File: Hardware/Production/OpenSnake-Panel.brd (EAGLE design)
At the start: 25.4 x 69.8 mm, 54 parts, among them Q1 16MHZ, U1 ATMEGA328P, U2 317

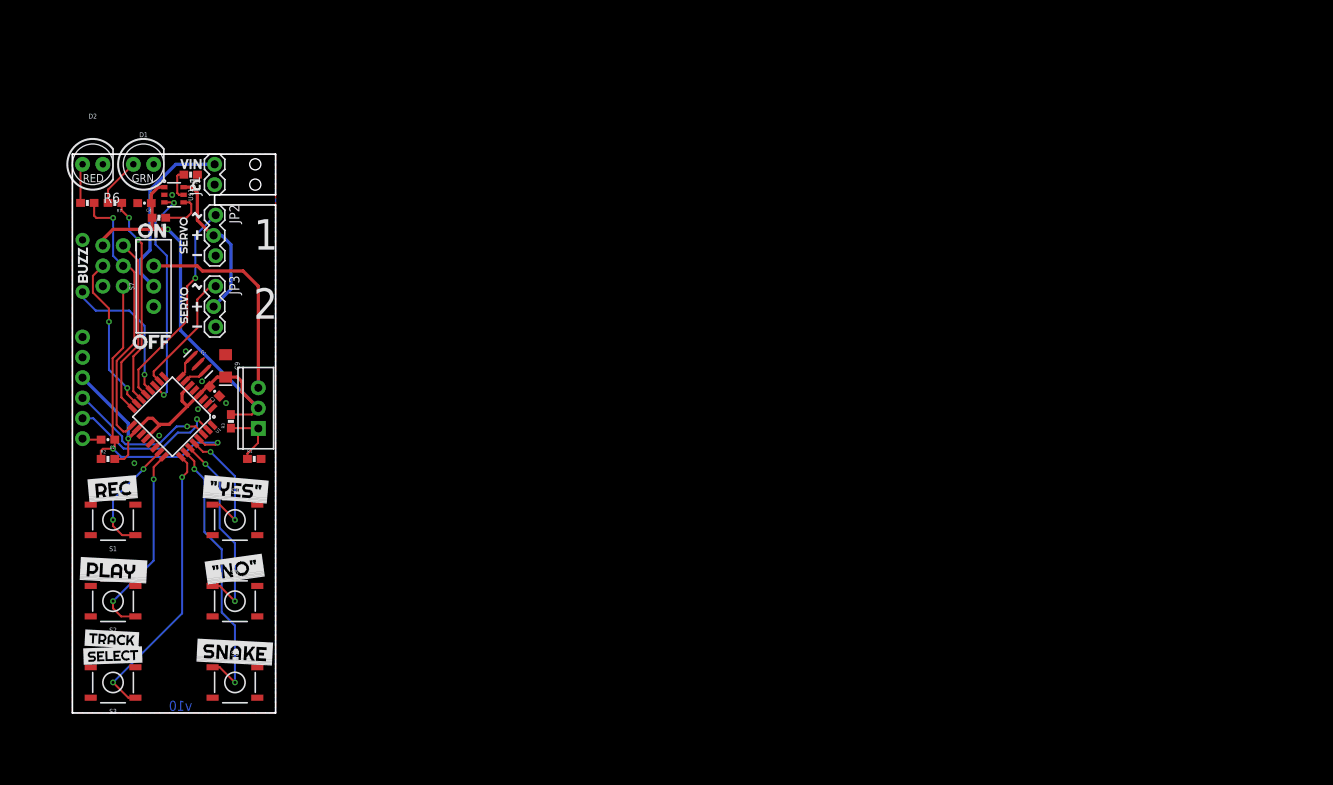
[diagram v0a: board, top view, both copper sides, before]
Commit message: final changes to v10
-added green LED
-added silk labels for servo ports
-Panelized and cammed
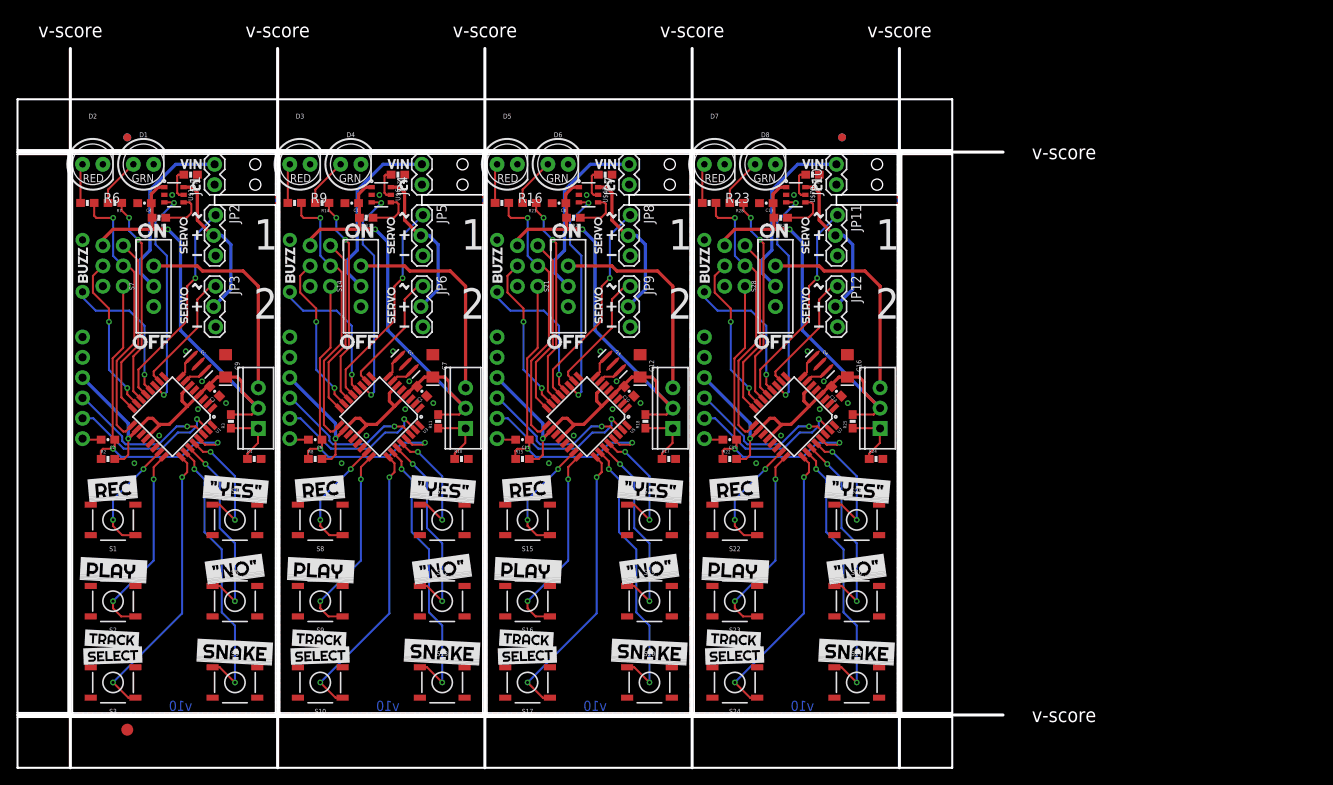
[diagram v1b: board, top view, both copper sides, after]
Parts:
- removed FRAME1: FRAME-LETTER, SparkFun-Aesthetics:CREATIVE_COMMONS
- added C1, C10, C11, C13, C14, C15, C5, C6, C8: 0.1uF, SparkFun-Capacitors:0603-CAP
- added C12, C16, C7: 10uF, SparkFun-Capacitors:EIA3216
- added D3, D5, D7: RED, SparkFun-LED:LED_5MM
- added D4, D6, D8: GREEN, SparkFun-LED:LED_5MM
- added E$1, E$2, E$3, E$4: (no value), SparkFun-Aesthetics:FIDUCIAL-1X2
- added E$5: (no value), SparkFun-Retired:FIDUCIAL-1.5X3
- added J3, J5, J7: (no value), SparkFun-Connectors:6_PIN_SERIAL_TARGET_SIDE_W_SILK
- added J4, J6, J8: (no value), SparkFun-Connectors:2X3
- added JP10, JP4, JP7: (no value), Testing:1X02
- added JP11, JP5, JP8: Servo 1, Testing:1X03_LOCK
- added JP12, JP6, JP9: Servo 2, Testing:1X03_LOCK
- added LOGO2, LOGO3, LOGO4: OSHW-LOGOL, SparkFun-Aesthetics:OSHW-LOGO-L
- added LS2, LS3, LS4: BUZZER, SparkFun-Electromechanical:BUZZER-12MM
- added Q2, Q3, Q4: 16MHZ, SparkFun-FreqCtrl:RESONATOR-SMD
- added R10, R17, R24: 715, SparkFun-Resistors:0603-RES
- added R11, R18, R25: 240, SparkFun-Resistors:0603-RES
- added R12, R13, R15, R19, R20, R22, R26, R27, R8: 10K, SparkFun-Resistors:0603-RES
- added R14, R16, R21, R23, R28, R9: 330, SparkFun-Resistors:0603-RES
- added S10, S11, S12, S13, S15, S16, S17, S18, S19, S20, S22, S23, S24, S25, S26, S27, S8, S9: (no value), SparkFun-Switches:TACTILE_SWITCH_SMD_5.2MM
- added S14, S21, S28: (no value), SparkFun-Switches:SWITCH_SPDT_PTH_11.6X4.0MM
- added U$25, U$48, U$71: (no value), buzzard_labels:#YES#0
- added U$26, U$49, U$72: (no value), buzzard_labels:#NO#1
- added U$27, U$50, U$73: (no value), buzzard_labels:SNAKE2
- added U$28, U$51, U$74: (no value), buzzard_labels (1):ON0
- added U$29, U$52, U$75: (no value), buzzard_labels (1):OFF1
- added U$30, U$53, U$76: (no value), buzzard_labels (1):VIN6
- added U$31, U$54, U$77: (no value), buzzard_labels (1):G8
- added U$32, U$55, U$78: (no value), buzzard_labels (2):REC0
- added U$33, U$56, U$79: (no value), buzzard_labels (2):PLAY_1
- added U$34, U$57, U$80: (no value), buzzard_labels (2):TRACK2
- added U$35, U$58, U$81: (no value), buzzard_labels (2):SELECT3
- added U$36, U$59, U$82: (no value), snake:MARIO_LOGO
- added U$37, U$60, U$83: (no value), buzzard_labels (4):BUZZ0
- added U$38, U$39, U$61, U$62, U$84, U$85: (no value), buzzard_labels (6):#1
- added U$40, U$41, U$63, U$64, U$86, U$87: (no value), buzzard_labels (6):SERVO2
- added U$42, U$65, U$88: (no value), buzzard_labels (7):SNAKE0
- added U$43, U$66, U$89: (no value), buzzard_labels (7):IN1
- added U$44, U$67, U$90: (no value), buzzard_labels (7):A2
- added U$45, U$68, U$91: (no value), buzzard_labels (7):CAN3
- added U$46, U$69, U$92: (no value), buzzard_labels (7):CONTROLLER4
- added U$47, U$6, U$70: (no value), snake:SOT26
- added U3, U5, U7: ATMEGA328P, SparkFun-DigitalIC:TQFP32-08
- added U4, U6, U8: 317, SparkFun-IC-Power:TO220-ADJ
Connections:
- new net !DTR1: C6.2, J3.P$1
- new net !DTR2: C11.2, J5.P$1
- new net !DTR3: C15.2, J7.P$1
- new net BUZZER1: LS2.+, U3.12
- new net BUZZER2: LS3.+, U5.12
- new net BUZZER3: LS4.+, U7.12
- new net D1: U3.32
- new net D3: U5.32
- new net D4: U7.32
- new net ENABLE_SERVO1: U$6.3, U3.11
- new net ENABLE_SERVO2: U$47.3, U5.11
- new net ENABLE_SERVO3: U$70.3, U7.11
- new net GND1: C1.2, C5.1, C7.-, D3.K, D4.K, J3.P$5, J3.P$6, J4.6, JP4.1, JP5.3, JP6.3, LS2.-, Q2.2, R10.2, R12.1, S10.3, S11.3, S12.3, S13.3, S8.3, S9.3, U$6.2, U3.21, U3.3, U3.5
- new net GND2: C10.1, C12.-, C8.2, D5.K, D6.K, J5.P$5, J5.P$6, J6.6, JP7.1, JP8.3, JP9.3, LS3.-, Q3.2, R17.2, R19.1, S15.3, S16.3, S17.3, S18.3, S19.3, S20.3, U$47.2, U5.21, U5.3, U5.5
- new net GND3: C13.2, C14.1, C16.-, D7.K, D8.K, J7.P$5, J7.P$6, J8.6, JP10.1, JP11.3, JP12.3, LS4.-, Q4.2, R24.2, R26.1, S22.3, S23.3, S24.3, S25.3, S26.3, S27.3, U$70.2, U7.21, U7.3, U7.5
- new net GRN_LED1: R14.1, U3.14
- new net GRN_LED2: R21.1, U5.14
- new net GRN_LED3: R28.1, U7.14
- new net MISO1: J4.1, U3.16
- new net MISO2: J6.1, U5.16
- new net MISO3: J8.1, U7.16
- new net MOSI1: J4.4, U3.15
- new net MOSI2: J6.4, U5.15
- new net MOSI3: J8.4, U7.15
- new net N$11: D3.A, R9.2
- new net N$12: Q2.1, U3.8
- new net N$13: Q2.3, U3.7
- new net N$14: R10.1, R11.1, U4.ADJ
- new net N$15: JP4.2, S14.2
- new net N$16: S14.1, U4.IN
- new net N$17: JP5.2, JP6.2, U$6.6
- new net N$18: R12.2, U$6.5
- new net N$19: R13.1, U$6.4
- new net N$20: D4.A, R14.2
- new net N$21: D5.A, R16.2
- new net N$22: Q3.1, U5.8
- new net N$23: Q3.3, U5.7
- new net N$24: R17.1, R18.1, U6.ADJ
- new net N$25: JP7.2, S21.2
- new net N$26: S21.1, U6.IN
- new net N$27: JP8.2, JP9.2, U$47.6
- new net N$28: R19.2, U$47.5
- new net N$29: R20.1, U$47.4
- new net N$30: D6.A, R21.2
- new net N$31: D7.A, R23.2
- new net N$32: Q4.1, U7.8
- new net N$33: Q4.3, U7.7
- new net N$34: R24.1, R25.1, U8.ADJ
- new net N$35: JP10.2, S28.2
- new net N$36: S28.1, U8.IN
- new net N$37: JP11.2, JP12.2, U$70.6
- new net N$38: R26.2, U$70.5
- new net N$39: R27.1, U$70.4
- new net N$40: D8.A, R28.2
- new net NO1: S12.1, U3.27
- new net NO2: S19.1, U5.27
- new net NO3: S26.1, U7.27
- new net PLAY1: S9.1, U3.24
- new net PLAY2: S16.1, U5.24
- new net PLAY3: S23.1, U7.24
- new net REC1: S8.1, U3.23
- new net REC2: S15.1, U5.23
- new net REC3: S22.1, U7.23
- new net RST1: C6.1, J4.5, R8.1, U3.29
- new net RST2: C11.1, J6.5, R15.1, U5.29
- new net RST3: C15.1, J8.5, R22.1, U7.29
- new net RX1: J3.P$3, U3.30
- new net RX2: J5.P$3, U5.30
- new net RX3: J7.P$3, U7.30
- new net SCK1: J4.3, R9.1, U3.17
- new net SCK2: J6.3, R16.1, U5.17
- new net SCK3: J8.3, R23.1, U7.17
- new net SERVO_3: JP5.1, U3.13
- new net SERVO_4: JP6.1, U3.10
- new net SERVO_5: JP8.1, U5.13
- new net SERVO_6: JP9.1, U5.10
- new net SERVO_7: JP11.1, U7.13
- new net SERVO_8: JP12.1, U7.10
- new net SNAKE1: S13.1, U3.26
- new net SNAKE2: S20.1, U5.26
- new net SNAKE3: S27.1, U7.26
- new net TRCK_SEL1: S10.1, U3.25
- new net TRCK_SEL2: S17.1, U5.25
- new net TRCK_SEL3: S24.1, U7.25
- new net TX1: J3.P$2, U3.31
- new net TX2: J5.P$2, U5.31
- new net TX3: J7.P$2, U7.31
- new net VCC1: C1.1, C5.2, C7.+, J3.P$4, J4.2, R11.2, R13.2, R8.2, U$6.1, U3.18, U3.20, U3.4, U3.6, U4.OUT
- new net VCC2: C10.2, C12.+, C8.1, J5.P$4, J6.2, R15.2, R18.2, R20.2, U$47.1, U5.18, U5.20, U5.4, U5.6, U6.OUT
- new net VCC3: C13.1, C14.2, C16.+, J7.P$4, J8.2, R22.2, R25.2, R27.2, U$70.1, U7.18, U7.20, U7.4, U7.6, U8.OUT
- new net YES1: S11.1, U3.28
- new net YES2: S18.1, U5.28
- new net YES3: S25.1, U7.28
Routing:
- net VCC3: track 0.00 -> 91.3 mm, vias 0 -> 2
- net VCC2: track 0.00 -> 91.3 mm, vias 0 -> 2
- net VCC1: track 0.00 -> 91.3 mm, vias 0 -> 2
- net RST3: track 0.00 -> 40.7 mm, vias 0 -> 2
- net RST2: track 0.00 -> 40.7 mm, vias 0 -> 2
- net RST1: track 0.00 -> 40.7 mm, vias 0 -> 2
- net TRCK_SEL3: track 0.00 -> 36.0 mm, vias 0 -> 2
- net TRCK_SEL2: track 0.00 -> 36.0 mm, vias 0 -> 2
- net TRCK_SEL1: track 0.00 -> 36.0 mm, vias 0 -> 2
- net SCK3: track 0.00 -> 35.0 mm, vias 0 -> 1
- net SCK2: track 0.00 -> 35.0 mm, vias 0 -> 1
- net SCK1: track 0.00 -> 35.0 mm, vias 0 -> 1
- net SNAKE1: track 0.00 -> 34.9 mm, vias 0 -> 2
- net SNAKE3: track 0.00 -> 34.9 mm, vias 0 -> 2
- net SNAKE2: track 0.00 -> 34.9 mm, vias 0 -> 2
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- added copper zone on layer 1, net GND1
- added copper zone on layer 16, net GND1
- added copper zone on layer 1, net GND2
- added copper zone on layer 16, net GND2
- added copper zone on layer 1, net GND3
- added copper zone on layer 16, net GND3
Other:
- board size 25.4 x 69.8 mm -> 123.2 x 89.9 mm
- board text added: "v-score"
- board text removed: "9V Battery"
- board text removed: "HINGE"
- board text removed: "Pete Lewis"
- board text removed: "cable to 9V battery"
- board text removed: "cable to servo 1"
- board text removed: "cable to servo 2"
- board text removed: "servo"

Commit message: v20 PCB layout - all SMD
-Moved to high side switch with mosfet for servo power control, this will also come directly from battery (since it is now max 6V) to alleviate vreg
-Switched to JST connector for batter input.
-removed power switch, because the plan is to source a battery holder with switch.
-moved to MIC5205 5V vreg, because it no longer has to power servo.
-switched to test points for programming to make room.
-SMD buzzer
-SMD LEDs
-SMD servo connectors
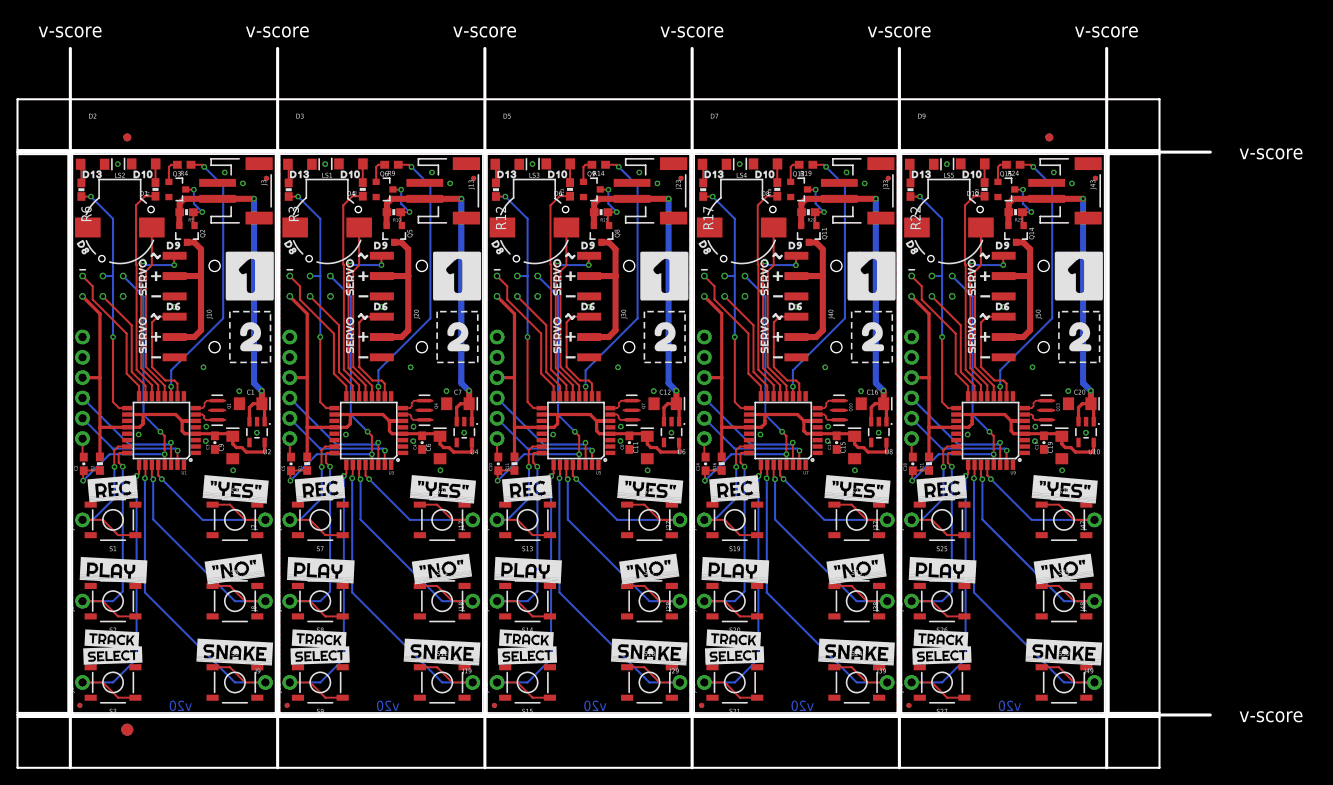
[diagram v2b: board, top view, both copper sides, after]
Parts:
- removed JP1, JP10, JP4, JP7: (no value), Testing:1X02
- removed JP11, JP2, JP5, JP8: Servo 1, Testing:1X03_LOCK
- removed JP12, JP3, JP6, JP9: Servo 2, Testing:1X03_LOCK
- removed R26, R27: 10K, SparkFun-Resistors:0603-RES
- removed R28: 330, SparkFun-Resistors:0603-RES
- added C17, C18: 0.1uF, SparkFun-Capacitors:0603-CAP
- added C19, C20: 10uF, SparkFun-Capacitors:EIA3216
- added D10: GREEN, SparkFun-LED:LED-1206
- added D9: RED, SparkFun-LED:LED-1206
- added E$6: (no value), SparkFun-Retired:FIDUCIAL-1.5X3
- added FD1, FD10, FD11, FD12, FD13, FD14, FD15, FD16, FD17, FD18, FD19, FD2, FD20, FD3, FD4, FD5, FD6, FD7, FD8, FD9: FIDUCIALUFIDUCIAL, SparkFun-Aesthetics:FIDUCIAL-MICRO
- added J10, J20, J30, J40, J50: RA 6Pin SMD, SparkFun-Connectors:1X06-SMD_RA_MALE
- added J11, J21, J31, J41: (no value), SparkFun-Connectors:6_PIN_SERIAL_TARGET_SIDE_W_SILK
- added J12, J22, J32, J42: SPI, SparkFun-Connectors:2X3_TEST_POINTS
- added J13, J23, J33, J43: (no value), SparkFun-Connectors:JST-2-SMD
- added J14, J15, J16, J17, J18, J19, J24, J25, J26, J27, J28, J29, J34, J35, J36, J37, J38, J39, J44, J45, J46, J47, J48, J49, J9: (no value), SparkFun-Connectors:1X01_NO_SILK
- added LOGO5: OSHW-LOGOL, SparkFun-Aesthetics:OSHW-LOGO-L
- added LS5: BUZZER, SparkFun-Electromechanical:BUZZER-CCV
- added Q10, Q13, Q7: 16MHZ, SparkFun-FreqCtrl:RESONATOR-SMD
- added Q11, Q14, Q5, Q8: 20V/4.2A/52mΩ/1.4W, SparkFun-DiscreteSemi:SOT23-3
- added Q12, Q15, Q6, Q9: 600mA/40V, SparkFun-DiscreteSemi:SOT23-3
- added S29, S30: (no value), SparkFun-Switches:TACTILE_SWITCH_SMD_5.2MM
- added U$100, U$129, U$130, U$99: (no value), buzzard_labels (6):#1
- added U$101, U$102, U$131, U$132: (no value), buzzard_labels (6):SERVO2
- added U$103, U$133: (no value), buzzard_labels (7):SNAKE0
- added U$104, U$134: (no value), buzzard_labels (7):IN1
- added U$105, U$135: (no value), buzzard_labels (7):A2
- added U$106, U$136: (no value), buzzard_labels (7):CAN3
- added U$107, U$137: (no value), buzzard_labels (7):CONTROLLER4
- added U$108, U$138: (no value), output:#A0#0
- added U$109, U$139: (no value), output:#A1#0
- added U$110, U$140: (no value), output:#A2#0
- added U$111, U$141: (no value), output:#A3#0
- added U$112, U$142: (no value), output:#A4#0
- added U$113, U$143: (no value), output:#A5#0
- added U$114, U$144: (no value), output:D90
- added U$115, U$145: (no value), output:D60
- added U$116, U$146: (no value), output:D100
- added U$117, U$147: (no value), output:D130
- added U$118, U$148: (no value), output:D80
- added U$119, U$149: (no value), output:#1#0
- added U$120, U$150: (no value), output:2_0
- added U$121: (no value), buzzard_labels:#YES#0
- added U$122: (no value), buzzard_labels:#NO#1
- added U$123, U$93: (no value), buzzard_labels:SNAKE2
- added U$124, U$94: (no value), buzzard_labels (2):REC0
- added U$125, U$95: (no value), buzzard_labels (2):PLAY_1
- added U$126, U$96: (no value), buzzard_labels (2):TRACK2
- added U$127, U$97: (no value), buzzard_labels (2):SELECT3
- added U$128, U$98: (no value), snake:MARIO_LOGO
- added U10: 5V, SparkFun-IC-Power:SOT23-5
- added U9: ATMEGA328P, SparkFun-DigitalIC:TQFP32-08
- C1, C11, C15, C6: value 0.1uF -> 10uF; device SparkFun-Capacitors:0603-CAP -> SparkFun-Capacitors:EIA3216
- D1, D2, D3, D4, D5, D6, D7, D8: device SparkFun-LED:LED_5MM -> SparkFun-LED:LED-1206
- J2: value (none) -> SPI; device SparkFun-Connectors:2X3 -> SparkFun-Connectors:2X3_TEST_POINTS
- J3: device SparkFun-Connectors:6_PIN_SERIAL_TARGET_SIDE_W_SILK -> SparkFun-Connectors:JST-2-SMD
- J4, J6, J8: device SparkFun-Connectors:2X3 -> SparkFun-Connectors:1X01_NO_SILK
- J5, J7: device SparkFun-Connectors:6_PIN_SERIAL_TARGET_SIDE_W_SILK -> SparkFun-Connectors:1X01_NO_SILK
- LS1, LS2, LS3, LS4: device SparkFun-Electromechanical:BUZZER-12MM -> SparkFun-Electromechanical:BUZZER-CCV
- Q2: value 16MHZ -> 20V/4.2A/52mΩ/1.4W; device SparkFun-FreqCtrl:RESONATOR-SMD -> SparkFun-DiscreteSemi:SOT23-3
- Q3: value 16MHZ -> 600mA/40V; device SparkFun-FreqCtrl:RESONATOR-SMD -> SparkFun-DiscreteSemi:SOT23-3
- R1, R10: value 715 -> 10K
- R11, R25: value 240 -> 10K
- R12, R13, R22, R8: value 10K -> 330
- R14, R9: value 330 -> 100; device SparkFun-Resistors:0603-RES -> SparkFun-Resistors:0603
- R16, R21: value 330 -> 10K
- R17: value 715 -> 330
- R18, R3: value 240 -> 330
- R19, R4: value 10K -> 100; device SparkFun-Resistors:0603-RES -> SparkFun-Resistors:0603
- R24: value 715 -> 100; device SparkFun-Resistors:0603-RES -> SparkFun-Resistors:0603
- S14, S21, S28, S7: device SparkFun-Switches:SWITCH_SPDT_PTH_11.6X4.0MM -> SparkFun-Switches:TACTILE_SWITCH_SMD_5.2MM
- U$1: device snake:SOT26 -> output:#A0#0
- U$10, U$52: device buzzard_labels (1):OFF1 -> output:#A4#0
- U$17, U$53: device buzzard_labels (1):VIN6 -> output:#A5#0
- U$18, U$54: device buzzard_labels (1):G8 -> output:D90
- U$25: device buzzard_labels:#YES#0 -> output:D60
- U$26: device buzzard_labels:#NO#1 -> output:D100
- U$27: device buzzard_labels:SNAKE2 -> output:D130
- U$28: device buzzard_labels (1):ON0 -> output:D80
- U$29: device buzzard_labels (1):OFF1 -> output:#1#0
- U$30: device buzzard_labels (1):VIN6 -> buzzard_labels:#YES#0
- U$31: device buzzard_labels (1):G8 -> output:2_0
- U$32: device buzzard_labels (2):REC0 -> buzzard_labels:#NO#1
- U$33: device buzzard_labels (2):PLAY_1 -> buzzard_labels:SNAKE2
- U$34: device buzzard_labels (2):TRACK2 -> buzzard_labels (2):REC0
- U$35: device buzzard_labels (2):SELECT3 -> buzzard_labels (2):PLAY_1
- U$36: device snake:MARIO_LOGO -> buzzard_labels (2):TRACK2
- U$37: device buzzard_labels (4):BUZZ0 -> buzzard_labels (2):SELECT3
- U$38: device buzzard_labels (6):#1 -> snake:MARIO_LOGO
- U$40: device buzzard_labels (6):SERVO2 -> buzzard_labels (6):#1
- U$42: device buzzard_labels (7):SNAKE0 -> buzzard_labels (6):SERVO2
- U$43: device buzzard_labels (7):IN1 -> buzzard_labels (7):SNAKE0
- U$44: device buzzard_labels (7):A2 -> buzzard_labels (7):IN1
- U$45: device buzzard_labels (7):CAN3 -> buzzard_labels (7):A2
- U$46: device buzzard_labels (7):CONTROLLER4 -> buzzard_labels (7):CAN3
- U$47: device snake:SOT26 -> buzzard_labels (7):CONTROLLER4
- U$48: device buzzard_labels:#YES#0 -> output:#A0#0
- U$49: device buzzard_labels:#NO#1 -> output:#A1#0
- U$50: device buzzard_labels:SNAKE2 -> output:#A2#0
- U$51, U$9: device buzzard_labels (1):ON0 -> output:#A3#0
- U$55: device buzzard_labels (2):REC0 -> output:D60
- U$56: device buzzard_labels (2):PLAY_1 -> output:D100
- U$57: device buzzard_labels (2):TRACK2 -> output:D130
- U$58: device buzzard_labels (2):SELECT3 -> output:D80
- U$59: device snake:MARIO_LOGO -> output:#1#0
- U$6: device snake:SOT26 -> output:#A1#0
- U$60: device buzzard_labels (4):BUZZ0 -> output:2_0
- U$61: device buzzard_labels (6):#1 -> buzzard_labels:#YES#0
- U$62: device buzzard_labels (6):#1 -> buzzard_labels:#NO#1
- U$63: device buzzard_labels (6):SERVO2 -> buzzard_labels:SNAKE2
- U$64: device buzzard_labels (6):SERVO2 -> buzzard_labels (2):REC0
- U$65: device buzzard_labels (7):SNAKE0 -> buzzard_labels (2):PLAY_1
- U$66: device buzzard_labels (7):IN1 -> buzzard_labels (2):TRACK2
- U$67: device buzzard_labels (7):A2 -> buzzard_labels (2):SELECT3
- U$68: device buzzard_labels (7):CAN3 -> snake:MARIO_LOGO
- U$69: device buzzard_labels (7):CONTROLLER4 -> buzzard_labels (6):#1
- U$7: device buzzard_labels (4):BUZZ0 -> output:#A2#0
- U$70: device snake:SOT26 -> buzzard_labels (6):#1
- U$71: device buzzard_labels:#YES#0 -> buzzard_labels (6):SERVO2
- U$72: device buzzard_labels:#NO#1 -> buzzard_labels (6):SERVO2
- U$73: device buzzard_labels:SNAKE2 -> buzzard_labels (7):SNAKE0
- U$74: device buzzard_labels (1):ON0 -> buzzard_labels (7):IN1
- U$75: device buzzard_labels (1):OFF1 -> buzzard_labels (7):A2
- U$76: device buzzard_labels (1):VIN6 -> buzzard_labels (7):CAN3
- U$77: device buzzard_labels (1):G8 -> buzzard_labels (7):CONTROLLER4
- U$78: device buzzard_labels (2):REC0 -> output:#A0#0
- U$79: device buzzard_labels (2):PLAY_1 -> output:#A1#0
- U$80: device buzzard_labels (2):TRACK2 -> output:#A2#0
- U$81: device buzzard_labels (2):SELECT3 -> output:#A3#0
- U$82: device snake:MARIO_LOGO -> output:#A4#0
- U$83: device buzzard_labels (4):BUZZ0 -> output:#A5#0
- U$84: device buzzard_labels (6):#1 -> output:D90
- U$85: device buzzard_labels (6):#1 -> output:D60
- U$86: device buzzard_labels (6):SERVO2 -> output:D100
- U$87: device buzzard_labels (6):SERVO2 -> output:D130
- U$88: device buzzard_labels (7):SNAKE0 -> output:D80
- U$89: device buzzard_labels (7):IN1 -> output:#1#0
- U$90: device buzzard_labels (7):A2 -> output:2_0
- U$91: device buzzard_labels (7):CAN3 -> buzzard_labels:#YES#0
- U$92: device buzzard_labels (7):CONTROLLER4 -> buzzard_labels:#NO#1
- U2, U4, U6, U8: value 317 -> 5V; device SparkFun-IC-Power:TO220-ADJ -> SparkFun-IC-Power:SOT23-5
- moved J6 78.9 mm to (1.27, 3.81), flipped to the top, turned to 90 degrees
- moved J8 74.6 mm to (24.1, 14.0), flipped to the top, turned to 90 degrees
- moved U$27 70.6 mm to (2.54, 67.3), turned to 0 degrees
- moved U$88 70.1 mm to (53.2, 58.1), flipped to the top, turned to 300 degrees
- moved U$6 63.0 mm to (1.27, 14.0), flipped to the bottom, turned to 0 degrees
- moved U$57 62.8 mm to (28.4, 67.3), turned to 0 degrees
- moved U$26 59.8 mm to (8.89, 67.3), turned to 0 degrees
- moved R21 59.6 mm to (107.1, 31.2), turned to 90 degrees
- moved U$9 59.2 mm to (24.1, 3.81), flipped to the bottom
- moved Q3 58.7 mm to (13.1, 65.4), turned to 270 degrees
- moved J5 58.3 mm to (1.27, 14.0), flipped to the top
- moved J7 57.3 mm to (24.1, 24.1), flipped to the top
- moved U$51 57.2 mm to (50.0, 3.81), flipped to the bottom
- moved U$58 57.0 mm to (27.3, 58.1), turned to 300 degrees
- moved U$59 54.5 mm to (43.6, 54.6), flipped to the top
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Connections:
- removed net N$36: S28.1, U8.IN
- removed net N$37: JP11.2, JP12.2, U$70.6
- removed net N$38: R26.2, U$70.5
- removed net N$39: R27.1, U$70.4
- removed net N$40: D8.A, R28.2
- new net !DTR4: C18.2, J41.P$1
- new net BUZZER4: LS5.-, U9.12
- new net D5: U9.32
- new net ENABLE_SERVO4: R24.1, U9.11
- new net GND4: C17.1, C19.-, C20.-, D10.C, D9.C, J41.P$5, J41.P$6, J42.6, J43.1, J50.1, J50.4, LS5.+, Q13.2, Q15.2, S25.3, S26.3, S27.3, S28.3, S29.3, S30.3, U10.2, U9.21, U9.3, U9.5
- new net GRN_LED4: R23.1, U9.14
- new net MISO4: J42.1, U9.16
- new net MOSI4: J42.4, U9.15
- new net NO4: J48.1, S29.1, U9.27
- new net PLAY4: J45.1, S26.1, U9.24
- new net REC4: J44.1, S25.1, U9.23
- new net RST4: C18.1, J42.5, R21.1, U9.29
- new net RX4: J41.P$3, U9.30
- new net SCK4: J42.3, R22.1, U9.17
- new net SERVO_10: J50.3, U9.10
- new net SERVO_9: J50.6, U9.13
- new net SNAKE4: J49.1, S30.1, U9.26
- new net TRCK_SEL4: J46.1, S27.1, U9.25
- new net TX4: J41.P$2, U9.31
- new net VBAT: C1.+, J3.2, Q2.2, R5.2, U2.1, U2.3
- new net VBAT1: C7.+, J13.2, Q5.2, R10.2, U4.1, U4.3
- new net VBAT2: C12.+, J23.2, Q8.2, R15.2, U6.1, U6.3
- new net VBAT3: C16.+, J33.2, Q11.2, R20.2, U8.1, U8.3
- new net VBAT4: C20.+, J43.2, Q14.2, R25.2, U10.1, U10.3
- new net VCC4: C17.2, C19.+, J41.P$4, J42.2, R21.2, U10.5, U9.18, U9.20, U9.4, U9.6
- new net YES4: J47.1, S28.1, U9.28
- net !DTR1: now also C5.2, J11.P$1; no longer C6.2, J3.P$1
- net !DTR2: now also C10.2, J21.P$1; no longer C11.2, J5.P$1
- net !DTR3: now also C14.2, J31.P$1; no longer C15.2, J7.P$1
- net BUZZER: now also LS2.-; no longer LS1.+
- net BUZZER1: now also LS1.-; no longer LS2.+
- net BUZZER2: now also LS3.-; no longer LS3.+
- net BUZZER3: now also LS4.-; no longer LS4.+
- net ENABLE_SERVO: now also R4.1; no longer U$1.3
- net ENABLE_SERVO1: now also R9.1; no longer U$6.3
- net ENABLE_SERVO2: now also R14.1; no longer U$47.3
- net ENABLE_SERVO3: now also R19.1; no longer U$70.3
- net GND: now also C1.-, D1.C, D2.C, J10.1, J10.4, J3.1, LS2.+, Q3.2, U2.2; no longer C4.2, D1.K, D2.K, JP1.1, JP2.3, JP3.3, LS1.-, R1.2, R4.1, U$1.2
- net GND1: now also C4.1, C6.-, D3.C, D4.C, J11.P$5, J11.P$6, J12.6, J13.1, J20.1, J20.4, LS1.+, Q4.2, Q6.2, S7.3, U4.2; no longer C1.2, C5.1, D3.K, D4.K, J3.P$5, J3.P$6, J4.6, JP4.1, JP5.3, JP6.3, LS2.-, Q2.2, R10.2, R12.1, S13.3, U$6.2
- net GND2: now also C11.-, C8.1, D5.C, D6.C, J21.P$5, J21.P$6, J22.6, J23.1, J30.1, J30.4, LS3.+, Q7.2, Q9.2, S13.3, S14.3, U6.2; no longer C10.1, C8.2, D5.K, D6.K, J5.P$5, J5.P$6, J6.6, JP7.1, JP8.3, JP9.3, LS3.-, Q3.2, R17.2, R19.1, S19.3, S20.3, U$47.2
- net GND3: now also C13.1, C15.-, D7.C, D8.C, J31.P$5, J31.P$6, J32.6, J33.1, J40.1, J40.4, LS4.+, Q10.2, Q12.2, S19.3, S20.3, S21.3, U8.2; no longer C13.2, C14.1, D7.K, D8.K, J7.P$5, J7.P$6, J8.6, JP10.1, JP11.3, JP12.3, LS4.-, Q4.2, R24.2, R26.1, S25.3, S26.3, S27.3, U$70.2
- net GRN_LED1: now also R8.1; no longer R14.1
- net GRN_LED2: now also R13.1; no longer R21.1
- net GRN_LED3: now also R18.1; no longer R28.1
- net MISO1: now also J12.1; no longer J4.1
- net MISO2: now also J22.1; no longer J6.1
- net MISO3: now also J32.1; no longer J8.1
- net MOSI1: now also J12.4; no longer J4.4
- net MOSI2: now also J22.4; no longer J6.4
- net MOSI3: now also J32.4; no longer J8.4
- net N$11: now also J20.2, J20.5, Q5.3; no longer D3.A, R9.2
- net N$12: now also D4.A, R8.2; no longer Q2.1, U3.8
- net N$13: now also Q6.1, R9.2; no longer Q2.3, U3.7
- net N$14: now also Q5.1, Q6.3; no longer R11.1, U4.ADJ
- net N$15: now also D5.A, R12.2; no longer JP4.2, S14.2
- net N$16: now also Q7.1, U5.8; no longer S14.1, U4.IN
- net N$17: now also Q7.3, U5.7; no longer JP5.2, JP6.2, U$6.6
- net N$18: now also J30.2, J30.5, Q8.3; no longer R12.2, U$6.5
- net N$19: now also D6.A, R13.2; no longer R13.1, U$6.4
- net N$20: now also Q9.1; no longer D4.A
- net N$21: now also Q8.1, Q9.3, R15.1; no longer D5.A, R16.2
- net N$22: now also D7.A, R17.2; no longer Q3.1, U5.8
- net N$23: now also Q10.1, U7.8; no longer Q3.3, U5.7
- net N$24: now also Q10.3, U7.7; no longer R17.1, R18.1, U6.ADJ
- net N$25: now also J40.2, J40.5, Q11.3; no longer JP7.2, S21.2
- net N$26: now also D8.A, R18.2; no longer S21.1, U6.IN
- net N$27: now also Q12.1, R19.2; no longer JP8.2, JP9.2, U$47.6
- net N$28: now also Q11.1, Q12.3, R20.1; no longer R19.2, U$47.5
- net N$29: now also D9.A, R22.2; no longer R20.1, U$47.4
- net N$3: now also D3.A, R3.2; no longer R1.1, R3.1, U2.ADJ
- net N$30: now also Q13.1, U9.8; no longer D6.A, R21.2
- net N$31: now also Q13.3, U9.7; no longer D7.A, R23.2
- net N$32: now also J50.2, J50.5, Q14.3; no longer Q4.1, U7.8
- net N$33: now also D10.A, R23.2; no longer Q4.3, U7.7
- net N$34: now also Q15.1, R24.2; no longer R24.1, R25.1, U8.ADJ
- net N$35: now also Q14.1, Q15.3, R25.1; no longer JP10.2, S28.2
- net N$4: now also Q3.1, R4.2; no longer JP1.2, S7.2
- net N$5: now also Q2.1, Q3.3, R5.1; no longer S7.1, U2.IN
- net N$6: now also J10.2, J10.5, Q2.3; no longer JP2.2, JP3.2, U$1.6
- net N$8: now also Q4.1, U3.8; no longer R4.2, U$1.5
- net N$9: now also Q4.3, U3.7; no longer R5.1, U$1.4
- net NO: now also J8.1
- net NO1: now also J18.1, S11.1; no longer S12.1
- net NO2: now also J28.1, S17.1; no longer S19.1
- net NO3: now also J38.1, S23.1; no longer S26.1
- net PLAY: now also J5.1
- net PLAY1: now also J15.1, S8.1; no longer S9.1
- net PLAY2: now also J25.1, S14.1; no longer S16.1
- net PLAY3: now also J35.1, S20.1; no longer S23.1
- net REC: now also J4.1
- net REC1: now also J14.1, S7.1; no longer S8.1
- net REC2: now also J24.1, S13.1; no longer S15.1
- net REC3: now also J34.1, S19.1; no longer S22.1
- net RST1: now also C5.1, J12.5, R1.1; no longer C6.1, J4.5, R8.1
- net RST2: now also C10.1, J22.5, R11.1; no longer C11.1, J6.5, R15.1
- net RST3: now also C14.1, J32.5, R16.1; no longer C15.1, J8.5, R22.1
- net RX1: now also J11.P$3; no longer J3.P$3
- net RX2: now also J21.P$3; no longer J5.P$3
- net RX3: now also J31.P$3; no longer J7.P$3
- net SCK1: now also J12.3, R3.1; no longer J4.3, R9.1
- net SCK2: now also J22.3, R12.1; no longer J6.3, R16.1
- net SCK3: now also J32.3, R17.1; no longer J8.3, R23.1
- net SERVO_1: now also J10.6; no longer JP2.1
- net SERVO_2: now also J10.3; no longer JP3.1
- net SERVO_3: now also J20.6; no longer JP5.1
- net SERVO_4: now also J20.3; no longer JP6.1
- net SERVO_5: now also J30.6; no longer JP8.1
- net SERVO_6: now also J30.3; no longer JP9.1
- net SERVO_7: now also J40.6; no longer JP11.1
- net SERVO_8: now also J40.3; no longer JP12.1
- net SNAKE: now also J9.1
- net SNAKE1: now also J19.1, S12.1; no longer S13.1
- net SNAKE2: now also J29.1, S18.1; no longer S20.1
- net SNAKE3: now also J39.1, S24.1; no longer S27.1
- net TRCK_SEL: now also J6.1
- net TRCK_SEL1: now also J16.1, S9.1; no longer S10.1
- net TRCK_SEL2: now also J26.1, S15.1; no longer S17.1
- net TRCK_SEL3: now also J36.1, S21.1; no longer S24.1
- net TX1: now also J11.P$2; no longer J3.P$2
- net TX2: now also J21.P$2; no longer J5.P$2
- net TX3: now also J31.P$2; no longer J7.P$2
- net VCC: now also U2.5; no longer C4.1, R3.2, R5.2, U$1.1, U2.OUT
- net VCC1: now also C4.2, C6.+, J11.P$4, J12.2, R1.2, U4.5; no longer C1.1, C5.2, C7.+, J3.P$4, J4.2, R11.2, R13.2, R8.2, U$6.1, U4.OUT
- net VCC2: now also C11.+, C8.2, J21.P$4, J22.2, R11.2, U6.5; no longer C10.2, C12.+, C8.1, J5.P$4, J6.2, R15.2, R18.2, R20.2, U$47.1, U6.OUT
- net VCC3: now also C13.2, C15.+, J31.P$4, J32.2, R16.2, U8.5; no longer C13.1, C14.2, C16.+, J7.P$4, J8.2, R22.2, R25.2, R27.2, U$70.1, U8.OUT
- net YES: now also J7.1
- net YES1: now also J17.1, S10.1; no longer S11.1
- net YES2: now also J27.1, S16.1; no longer S18.1
- net YES3: now also J37.1, S22.1; no longer S25.1
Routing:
- net VCC4: track 0.00 -> 55.3 mm
- net VBAT2: track 0.00 -> 44.2 mm, vias 0 -> 2
- net VBAT3: track 0.00 -> 44.2 mm, vias 0 -> 2
- net VBAT: track 0.00 -> 44.2 mm, vias 0 -> 2
- net VBAT4: track 0.00 -> 44.2 mm, vias 0 -> 2
- net VBAT1: track 0.00 -> 44.2 mm, vias 0 -> 2
- net SNAKE4: track 0.00 -> 43.1 mm, vias 0 -> 1
- net RST4: track 0.00 -> 40.6 mm, vias 0 -> 3
- net TRCK_SEL4: track 0.00 -> 39.8 mm, vias 0 -> 1
- net VCC3: track 91.3 -> 55.3 mm, vias 2 -> 0
- net VCC2: track 91.3 -> 55.3 mm, vias 2 -> 0
- net VCC1: track 91.3 -> 55.3 mm, vias 2 -> 0
- net VCC: track 91.3 -> 55.3 mm, vias 2 -> 0
- net ENABLE_SERVO4: track 0.00 -> 34.1 mm, vias 0 -> 2
- net NO4: track 0.00 -> 32.5 mm, vias 0 -> 1
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- added copper zone on layer 1, net GND4
- added copper zone on layer 16, net GND4
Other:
- board size 123.2 x 89.9 mm -> 149.1 x 89.9 mm
- board text added: "v20"
- board text removed: "1"
- board text removed: "2"
- board text removed: "GRN"
- board text removed: "RED"
- board text removed: "v10"
